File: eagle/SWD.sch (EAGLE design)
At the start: 69 parts, among them IC1 FT231X, J1 POWER_JACKPTH, U1 OPENMV3-JIG, U2 OPENMV3-JIG, U2-32KB EEPROM-I2CSMD, U3 OPENMV3-JIG, U4 OPENMV3-JIG, U5 OPENMV3-JIG, X1 USB-MICROB, Y1 5MHz-20pF-30ppm

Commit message: * Update jig (see details)
* Make SWD resistors 100 ohms (RN5-RN2)
* Remove D1 (not really needed).
* Add propeller reset circuit.
* Change all pull-up resistors to 10K.
* Add more silkscreen labels (power switch, power LED, 5V input).
* Use different colors for the power LED, program LED, and board LEDs.
* Add jig instructions to the silk screen.
* Move power LED to be visible.
* Remove FT231x and use FTDI cable header.
* Terminate propeller TX.
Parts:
- removed C25, C26, C29: 0.1uF, sfe:CAP0603-CAP
- removed C27: 10uF, sfe:CAP_POL1206
- removed C28: 10nF, sfe:CAP0603-CAP
- removed D5, D6: (no value), sfe:LED0603
- removed D7: (no value), sfe:DIODESOD
- removed F1: PTC0603, sfe:PTC0603
- removed IC1: FT231X, iofault:FT231X
- removed IC2: (no value), sfe:V_REG_LM1117SOT223
- removed L1: (no value), sfe:INDUCTOR0603
- removed R18, R20: 220, sfe:RESISTOR0603-RES
- removed R21, R22: 27R, sfe:RESISTOR0603-RES
- removed U$12: USD-47571, mux:USD-47571
- removed X1: USB-MICROB, sfe:USB-MICROB
- added JP1: (no value), pinhead:PINHD-1X6
- added R4: 100R, sfe:RESISTOR0603-RES
- added U12: USD-47571, mux:USD-47571
- added U7: (no value), sfe:V_REG_LM1117SOT223
- D2: value DIODE-SCHOTTKY_ -> (none); device sfe:DIODE-SCHOTTKY_ -> sfe:DIODESOD
- LED1, LED3, LED4, LED5, LED6: value (none) -> GREEN
- LED2, LED8: value (none) -> RED
- R14, RN1, RN6, RN7: value 4.7K -> 10K
- RN2, RN3, RN4, RN5: value 50R -> 100R
- Y1: value 5MHz-20pF-30ppm -> 5MHz-18pF-30ppm
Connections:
- removed net 3V3: C26.1, C29.1, IC1.3V3OUT, IC1.RESET, IC1.VCCIO
- removed net CTS: IC1.CTS
- removed net DTR: D7.C, IC1.DTR
- removed net N$10: R22.1, X1.D+
- removed net N$11: F1.1, L1.2
- removed net N$17: D5.A, R18.2
- removed net N$8: R21.1, X1.D-
- removed net RXLED: D5.C, IC1.RXLED
- removed net TXLED: D6.C, IC1.TXLED
- removed net USBDM: IC1.USBDM, R21.2
- removed net USBDP: IC1.USBDP, R22.2
- removed net VBUS: C25.1, C27.+, C28.1, F1.2, IC1.VCC, R18.1, R20.1
- removed net VBUS_RAW: L1.1, X1.VBUS
- new net N$1: R4.1, U6P8X32A-Q44.P30
- net 3.3V: now also U12.VDD, U7.OUT; no longer D1.A, IC2.OUT, U$12.VDD
- net GND: now also JP1.1, U12.GND@1, U12.GND@2, U12.GND@3, U12.POL, U12.VSS, U7.OUT@1; no longer C25.2, C26.2, C27.-, C28.2, C29.2, IC1.GND16, IC1.GND6, IC2.OUT@1, U$12.GND@1, U$12.GND@2, U$12.GND@3, U$12.POL, U$12.VSS, X1.GND
- net N$12: now also U12.DAT1; no longer U$12.DAT1
- net N$13: now also U12.DAT2; no longer U$12.DAT2
- net N$2: now also D1.A; no longer D2.A
- net N$31: now also U7.ADJ; no longer IC2.ADJ
- net N$7: now also D2.A, U6P8X32A-Q44.RES/; no longer D6.A, R20.2
- net PROP_RESET: now also D2.C, JP1.6; no longer D7.A, U6P8X32A-Q44.RES/
- net SD_CD: now also U12.CD; no longer U$12.CD
- net SD_CLK: now also U12.CLK; no longer U$12.CLK
- net SD_CS: now also U12.DAT3/CD; no longer U$12.DAT3/CD
- net SD_DI: now also U12.CMD; no longer U$12.CMD
- net SD_DO: now also U12.DAT0; no longer U$12.DAT0
- net SERIAL_RX: now also JP1.4; no longer IC1.TXD
- net SERIAL_TX: now also JP1.5, R4.2; no longer IC1.RXD, U6P8X32A-Q44.P30
- net VIN: now also U7.IN; no longer D2.C, IC2.IN
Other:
- note added: "FTDI Cable"
- moved on the sheet: C1, C16, C17, C19, C2, C20, C21, C22, C23, C24, C3, C4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

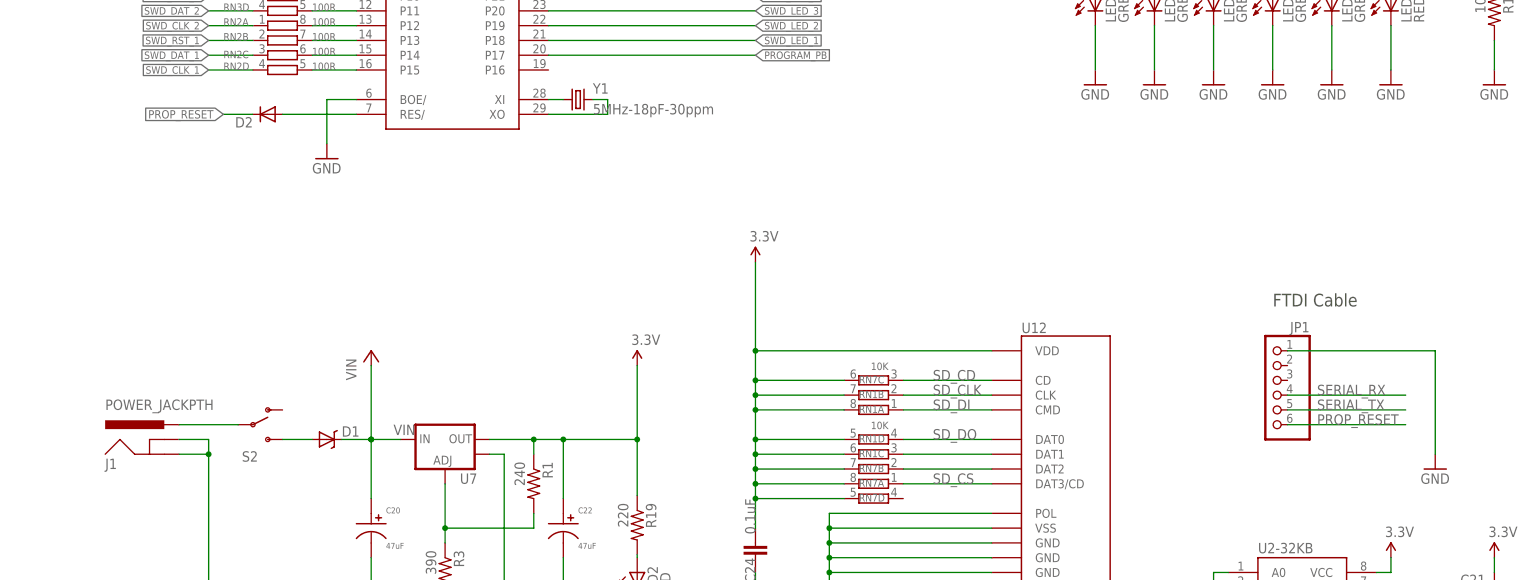
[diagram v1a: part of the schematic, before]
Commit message: Replace common parts with MF parts
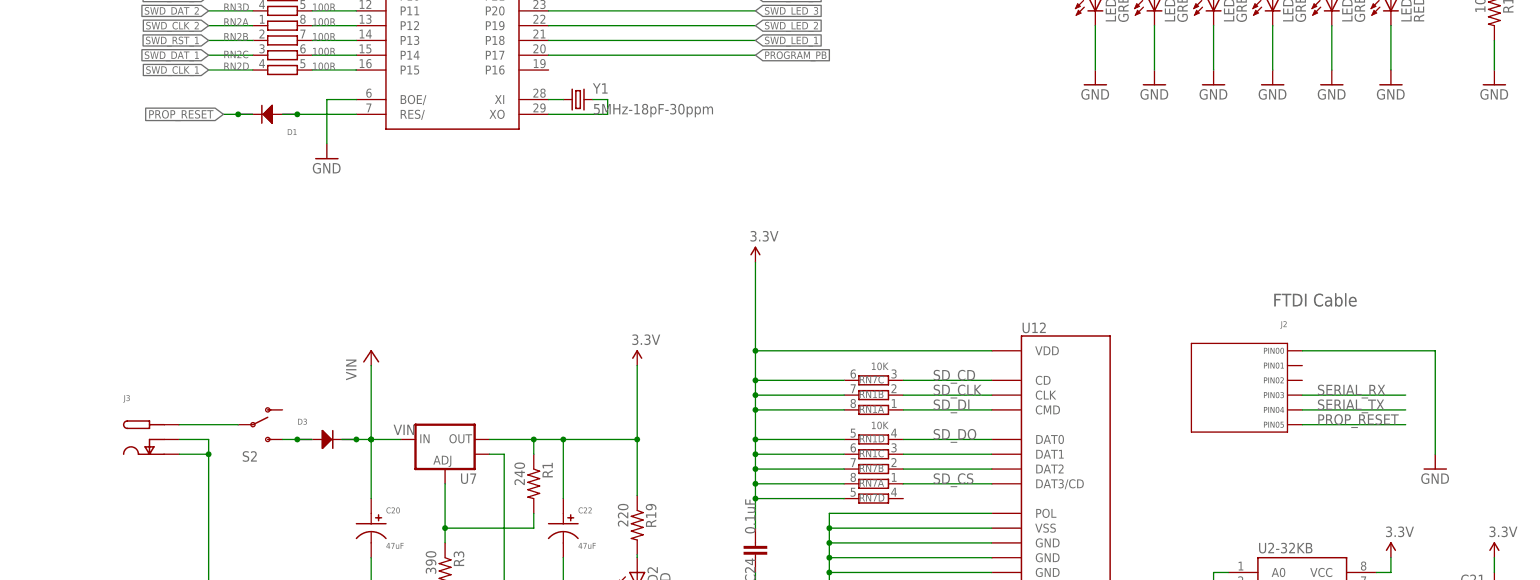
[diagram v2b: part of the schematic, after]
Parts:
- removed D2: (no value), sfe:DIODESOD
- removed J1: POWER_JACKPTH, sfe:POWER_JACKPTH
- removed JP1: (no value), pinhead:PINHD-1X6
- added D3: (no value), MF_Discrete_Semiconductor:DIODE_SMA
- added J2: (no value), MF_Connectors:HEADER_01X06_PTH_2.54MM
- added J3: (no value), MF_Connectors:DC_PWR_JACK_2.5MM_RIGHT
- D1: value DIODE-SCHOTTKY_ -> (none); device sfe:DIODE-SCHOTTKY_ -> MF_Discrete_Semiconductor:DIODE_SOD-123
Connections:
- net GND: now also J2.PIN0, J3.SLEEVE, J3.SLEEVE_SHUNT; no longer J1.GND, J1.GNDBREAK, JP1.1
- net N$2: now also D3.ANODE; no longer D1.A
- net N$7: now also D1.ANODE; no longer D2.A
- net N$9: now also J3.PIN; no longer J1.PWR
- net PROP_RESET: now also D1.CATHODE, J2.PIN5; no longer D2.C, JP1.6
- net SERIAL_RX: now also J2.PIN3; no longer JP1.4
- net SERIAL_TX: now also J2.PIN4; no longer JP1.5
- net VIN: now also D3.CATHODE; no longer D1.C
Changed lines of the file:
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@@
 <setting verticaltext="up"/>
 </settings>
-<grid distance="0.1" unitdist="inch" unit="inch" style="lines" multiple="1" display="yes" altdistance="0.01" altunitdist="inch" altunit="inch"/>
+<grid distance="0.1" unitdist="inch" unit="inch" style="lines" multiple="1" display="no" altdistance="0.01" altunitdist="inch" altunit="inch"/>
 <layers>
 <layer number="1" name="Top" color="4" fill="1" visible="no" active="no"/>
@@
 <part name="U5" library="openmv" deviceset="OPENMV3-JIG" device=""/>
 <part name="GND1" library="supply" deviceset="GND" device=""/>
-<part name="J1" library="sfe" deviceset="POWER_JACK" device="PTH"/>
 <part name="GND6" library="sfe" deviceset="GND" device=""/>
 <part name="GND30" library="sfe" deviceset="GND" device=""/>
@@
 <part name="R19" library="sfe" deviceset="RESISTOR" device="0603-RES" value="220"/>
 <part name="GND5" library="sfe" deviceset="GND" device=""/>
-<part name="D1" library="sfe" deviceset="DIODE-SCHOTTKY" device="_" value=""/>
 <part name="U7" library="sfe" deviceset="V_REG_LM1117" device="SOT223"/>
 <part name="R1" library="sfe" deviceset="RESISTOR" device="0603-RES" value="240"/>
@@
 <part name="GND10" library="sfe" deviceset="GND" device=""/>
 <part name="GND13" library="SparkFun-Aesthetics" deviceset="GND" device=""/>
-<part name="JP1" library="pinhead" deviceset="PINHD-1X6" device=""/>
 <part name="R4" library="sfe" deviceset="RESISTOR" device="0603-RES" value="100R"/>
-<part name="D2" library="sfe" deviceset="DIODE" device="SOD"/>
+<part name="J2" library="MF_Connectors" deviceset="HEADER_01X06" device="_PTH_2.54MM"/>
+<part name="D3" library="MF_Discrete_Semiconductor" deviceset="DIODE" device="_SMA"/>
+<part name="J3" library="MF_Connectors" deviceset="DC_PWR_JACK" device="_2.5MM_RIGHT"/>
+<part name="D1" library="MF_Discrete_Semiconductor" deviceset="DIODE" device="_SOD-123"/>
 </parts>
 <sheets>
@@
 <instance part="U5" gate="G$1" x="111.76" y="-149.86"/>
 <instance part="GND1" gate="1" x="66.04" y="-172.72"/>
-<instance part="J1" gate="G$1" x="-213.36" y="-139.7"/>
 <instance part="GND6" gate="1" x="-205.74" y="-167.64"/>
 <instance part="GND30" gate="1" x="-144.78" y="-167.64"/>
@@
 <instance part="R19" gate="G$1" x="-132.08" y="-149.352" rot="R270"/>
 <instance part="GND5" gate="1" x="-132.08" y="-167.64"/>
-<instance part="D1" gate="G$1" x="-185.42" y="-134.62"/>
 <instance part="U7" gate="G$1" x="-165.1" y="-134.62"/>
 <instance part="R1" gate="G$1" x="-149.86" y="-142.24" rot="R270"/>
@@
 <instance part="GND10" gate="1" x="-154.94" y="-167.64"/>
 <instance part="GND13" gate="1" x="5.08" y="-139.7"/>
-<instance part="JP1" gate="A" x="-22.86" y="-127" rot="MR0"/>
 <instance part="R4" gate="G$1" x="-142.24" y="-35.56"/>
-<instance part="D2" gate="G$1" x="-195.58" y="-78.74" rot="R180"/>
+<instance part="J2" gate="G$1" x="-20.32" y="-119.38" rot="MR0"/>
+<instance part="D3" gate="G$1" x="-185.42" y="-134.62"/>
+<instance part="J3" gate="G$1" x="-218.44" y="-134.62"/>
+<instance part="D1" gate="G$1" x="-195.58" y="-78.74" rot="R180"/>
 </instances>
 <busses>
@@
 <wire x1="-205.74" y1="-137.16" x2="-205.74" y2="-165.1" width="0.1524" layer="91"/>
 <junction x="-205.74" y="-137.16"/>
-<pinref part="J1" gate="G$1" pin="GNDBREAK"/>
-<pinref part="J1" gate="G$1" pin="GND"/>
 <pinref part="GND6" gate="1" pin="GND"/>
+<pinref part="J3" gate="G$1" pin="SLEEVE"/>
+<pinref part="J3" gate="G$1" pin="SLEEVE_SHUNT"/>
 </segment>
 <segment>
@@
 </segment>
 <segment>
-<wire x1="-20.32" y1="-119.38" x2="5.08" y2="-119.38" width="0.1524" layer="91"/>
+<wire x1="-17.78" y1="-119.38" x2="5.08" y2="-119.38" width="0.1524" layer="91"/>
 <wire x1="5.08" y1="-119.38" x2="5.08" y2="-137.16" width="0.1524" layer="91"/>
 <pinref part="GND13" gate="1" pin="GND"/>
-<pinref part="JP1" gate="A" pin="1"/>
+<pinref part="J2" gate="G$1" pin="PIN0"/>
 </segment>
 </net>
@@
 <segment>
 <wire x1="-210.82" y1="-132.08" x2="-200.66" y2="-132.08" width="0.1524" layer="91"/>
-<pinref part="J1" gate="G$1" pin="PWR"/>
 <pinref part="S2" gate="1" pin="P"/>
+<pinref part="J3" gate="G$1" pin="PIN"/>
 </segment>
 </net>
 <net name="N$2" class="0">
 <segment>
-<pinref part="D1" gate="G$1" pin="A"/>
-<wire x1="-187.96" y1="-134.62" x2="-193.04" y2="-134.62" width="0.1524" layer="91"/>
+<wire x1="-187.96" y1="-134.62" x2="-190.5" y2="-134.62" width="0.1524" layer="91"/>
 <pinref part="S2" gate="1" pin="S"/>
+<pinref part="D3" gate="G$1" pin="ANODE"/>
+<wire x1="-190.5" y1="-134.62" x2="-193.04" y2="-134.62" width="0.1524" layer="91"/>
+<junction x="-190.5" y="-134.62"/>
 </segment>
 </net>
@@
 </segment>
 <segment>
-<wire x1="-20.32" y1="-127" x2="0" y2="-127" width="0.1524" layer="91"/>
-<pinref part="JP1" gate="A" pin="4"/>
+<wire x1="-17.78" y1="-127" x2="0" y2="-127" width="0.1524" layer="91"/>
 <label x="-15.24" y="-127" size="1.778" layer="95"/>
+<pinref part="J2" gate="G$1" pin="PIN3"/>
 </segment>
 </net>
@@
 </segment>
 <segment>
-<wire x1="-20.32" y1="-129.54" x2="0" y2="-129.54" width="0.1524" layer="91"/>
-<pinref part="JP1" gate="A" pin="5"/>
+<wire x1="-17.78" y1="-129.54" x2="0" y2="-129.54" width="0.1524" layer="91"/>
 <label x="-15.24" y="-129.54" size="1.778" layer="95"/>
+<pinref part="J2" gate="G$1" pin="PIN4"/>
 </segment>
 </net>
@@
 <net name="VIN" class="0">
 <segment>
-<wire x1="-182.88" y1="-134.62" x2="-177.8" y2="-134.62" width="0.1524" layer="91"/>
+<wire x1="-182.88" y1="-134.62" x2="-180.34" y2="-134.62" width="0.1524" layer="91"/>
+<wire x1="-180.34" y1="-134.62" x2="-177.8" y2="-134.62" width="0.1524" layer="91"/>
 <wire x1="-177.8" y1="-134.62" x2="-172.72" y2="-134.62" width="0.1524" layer="91"/>
 <wire x1="-177.8" y1="-134.62" x2="-177.8" y2="-144.78" width="0.1524" layer="91"/>
@@
 <junction x="-177.8" y="-134.62"/>
 <label x="-170.18" y="-132.08" size="1.778" layer="95" rot="R180"/>
-<pinref part="D1" gate="G$1" pin="C"/>
 <pinref part="U7" gate="G$1" pin="IN"/>
 <pinref part="C20" gate="G$1" pin="P$1"/>
 <pinref part="VIN2" gate="G$1" pin="VIN"/>
 <wire x1="-177.8" y1="-134.62" x2="-177.8" y2="-121.92" width="0.1524" layer="91"/>
+<pinref part="D3" gate="G$1" pin="CATHODE"/>
+<junction x="-180.34" y="-134.62"/>
 </segment>
 <segment>
@@
 <net name="PROP_RESET" class="0">
 <segment>
-<pinref part="D2" gate="G$1" pin="C"/>
-<wire x1="-198.12" y1="-78.74" x2="-203.2" y2="-78.74" width="0.1524" layer="91"/>
+<wire x1="-198.12" y1="-78.74" x2="-200.66" y2="-78.74" width="0.1524" layer="91"/>
 <label x="-203.2" y="-78.74" size="1.4224" layer="95" rot="R180" xref="yes"/>
-</segment>
-<segment>
-<pinref part="JP1" gate="A" pin="6"/>
-<wire x1="-20.32" y1="-132.08" x2="0" y2="-132.08" width="0.1524" layer="91"/>
+<pinref part="D1" gate="G$1" pin="CATHODE"/>
+<wire x1="-200.66" y1="-78.74" x2="-203.2" y2="-78.74" width="0.1524" layer="91"/>
+<junction x="-200.66" y="-78.74"/>
+</segment>
+<segment>
+<wire x1="-17.78" y1="-132.08" x2="0" y2="-132.08" width="0.1524" layer="91"/>
 <label x="-15.24" y="-132.08" size="1.778" layer="95"/>
+<pinref part="J2" gate="G$1" pin="PIN5"/>
 </segment>
 </net>
@@
 <segment>
 <pinref part="U6" gate="P8X32A-Q44" pin="RES/"/>
-<pinref part="D2" gate="G$1" pin="A"/>
-<wire x1="-180.34" y1="-78.74" x2="-193.04" y2="-78.74" width="0.1524" layer="91"/>
-</segment>
-</net>
+<wire x1="-180.34" y1="-78.74" x2="-190.5" y2="-78.74" width="0.1524" layer="91"/>
+<pinref part="D1" gate="G$1" pin="ANODE"/>
+<wire x1="-190.5" y1="-78.74" x2="-193.04" y2="-78.74" width="0.1524" layer="91"/>
+<junction x="-190.5" y="-78.74"/>
+</segment>
+</net>
